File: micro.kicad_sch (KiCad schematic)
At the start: 13 parts, among them J7 USB_C_Receptacle_USB2.0_16P, J8 Conn_01x04_Pin, SW8 SW_Push, U4 ESP32-S3-WROOM-2

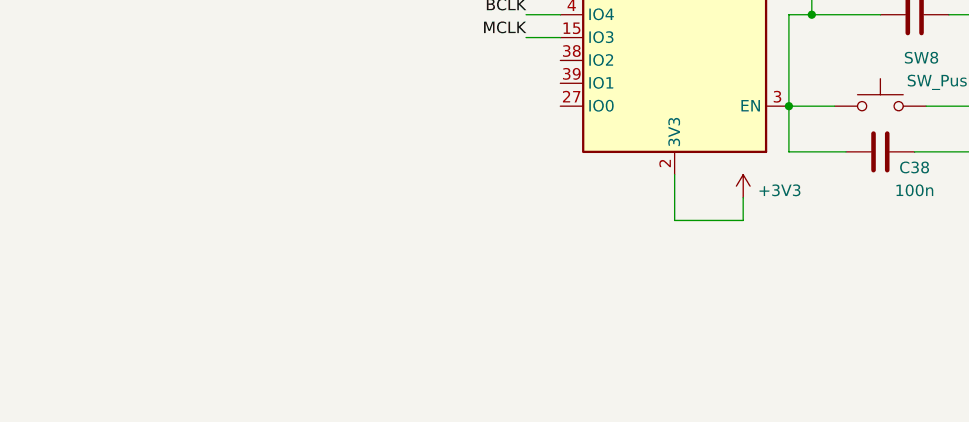
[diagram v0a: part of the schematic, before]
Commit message: aggiunto filtro PLL_LF Adau
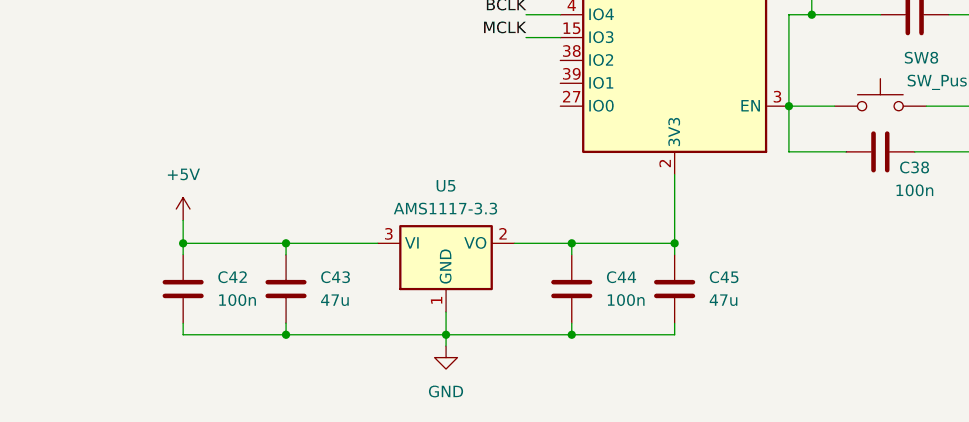
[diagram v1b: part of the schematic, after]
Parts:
- added C42, C44: 100n, Capacitor_SMD:C_0603_1608Metric, symbol Device:C
- added C43, C45: 47u, Capacitor_SMD:C_0603_1608Metric, symbol Device:C
- added U5: AMS1117-3.3, Package_TO_SOT_SMD:SOT-223-3_TabPin2, symbol Regulator_Linear:AMS1117-3.3
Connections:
- net +3V3: no longer U4.2 (3V3)
- net +5V: now also C42.1, C43.1, U5.3 (VI)
- net GND: now also C42.2, C43.2, C44.2, C45.2, U5.1 (GND)
- new net: C44.1, C45.1, U4.2 (3V3), U5.2 (VO)

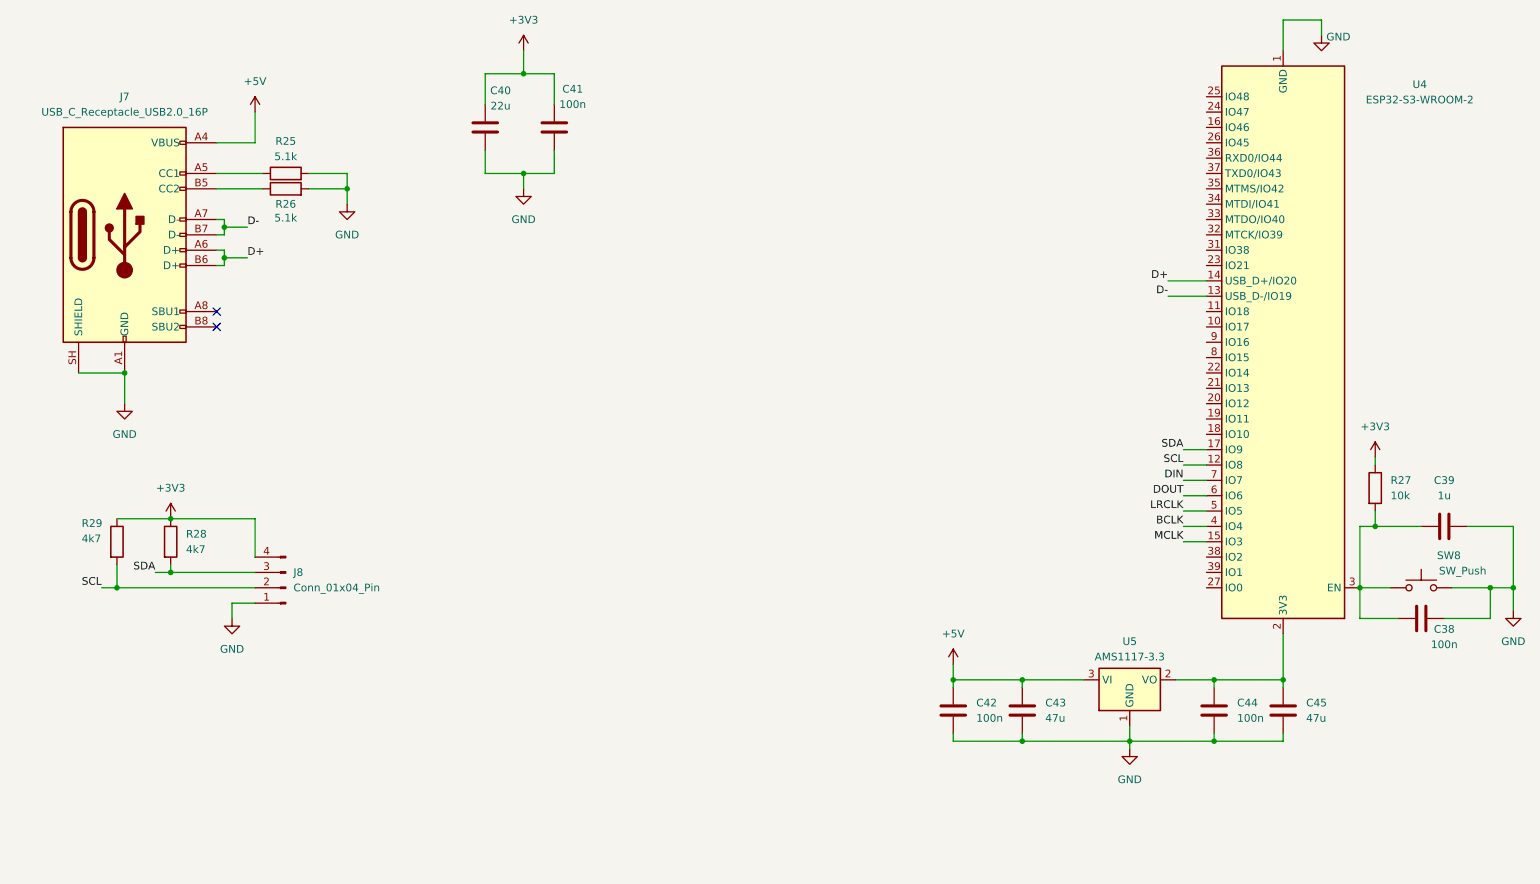
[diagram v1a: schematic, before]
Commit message: sostituito micro esp32 a stm32
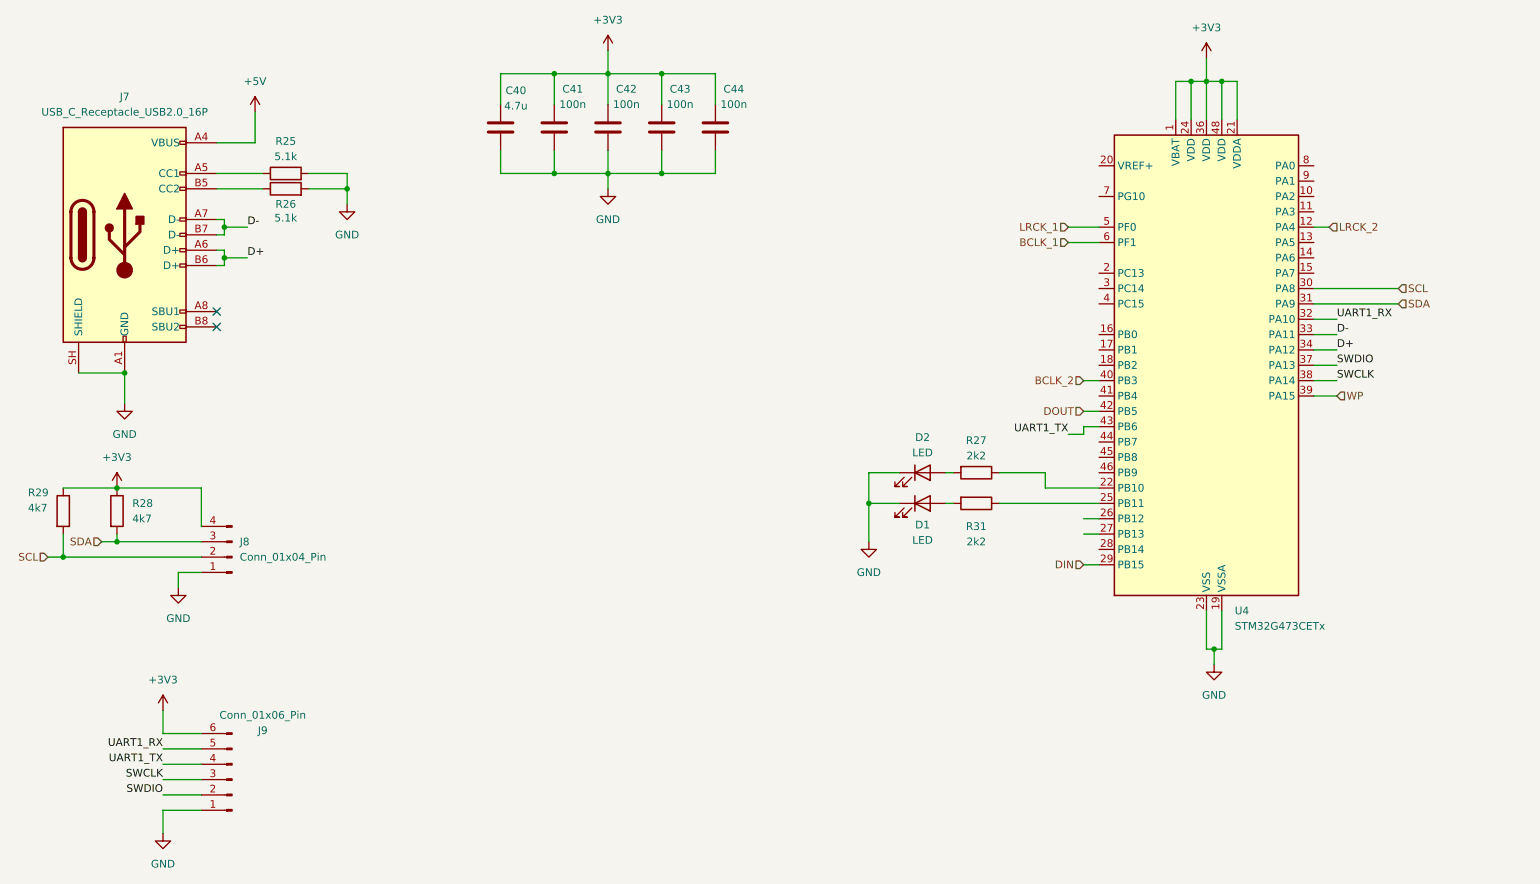
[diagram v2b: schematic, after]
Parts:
- removed C38: 100n, Capacitor_SMD:C_0603_1608Metric, symbol Device:C
- removed C39: 1u, Capacitor_SMD:C_0603_1608Metric, symbol Device:C
- removed C45: 47u, Capacitor_SMD:C_0603_1608Metric, symbol Device:C
- removed SW8: SW_Push, Button_Switch_SMD:SW_SPST_PTS645Sx43SMTR92, symbol Switch:SW_Push
- removed U4: ESP32-S3-WROOM-2, RF_Module:ESP32-S3-WROOM-2, symbol RF_Module:ESP32-S3-WROOM-2
- removed U5: AMS1117-3.3, Package_TO_SOT_SMD:SOT-223-3_TabPin2, symbol Regulator_Linear:AMS1117-3.3
- added D1, D2: LED, LED_SMD:LED_1210_3225Metric, symbol Device:LED
- added J9: Conn_01x06_Pin, Connector_JST:JST_XH_B6B-XH-A_1x06_P2.50mm_Vertical, symbol Connector:Conn_01x06_Pin
- added R31: 2k2, Resistor_SMD:R_0603_1608Metric, symbol Device:R
- added U4: STM32G473CETx, Package_QFP:LQFP-48_7x7mm_P0.5mm, symbol MCU_ST_STM32G4:STM32G473CETx
- C40: value 22u -> 4.7u
- C43: value 47u -> 100n
- R27: value 10k -> 2k2; footprint Capacitor_SMD:C_0603_1608Metric -> Resistor_SMD:R_0603_1608Metric
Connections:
- net +3V3: now also C42.1, C43.1, C44.1, J9.6 (Pin_6), U4.1 (VBAT), U4.21 (VDDA), U4.24 (VDD), U4.36 (VDD), U4.48 (VDD); no longer R27.1
- net +5V: no longer C42.1, C43.1
- net D+: now also U4.34 (PA12)
- net D-: now also U4.33 (PA11)
- net DIN: now also U4.29 (PB15)
- net DOUT: now also U4.42 (PB5)
- net GND: now also D1.1 (K), D2.1 (K), J9.1 (Pin_1), U4.19 (VSSA), U4.23 (VSS), U4.35 (VSS), U4.47 (VSS)
- net SCL: now also U4.30 (PA8)
- net SDA: now also U4.31 (PA9)
- net at R27.2: now also D2.2 (A)
- new net: R27.1, U4.22 (PB10)
- new net: R31.1, U4.25 (PB11)
- new net: D1.2 (A), R31.2
- new net BCLK_1: U4.6 (PF1)
- new net BCLK_2: U4.40 (PB3)
- new net LRCK_1: U4.5 (PF0)
- new net LRCK_2: U4.12 (PA4)
- new net SWCLK: J9.3 (Pin_3), U4.38 (PA14)
- new net SWDIO: J9.2 (Pin_2), U4.37 (PA13)
- new net UART1_RX: J9.5 (Pin_5), U4.32 (PA10)
- new net UART1_TX: J9.4 (Pin_4), U4.43 (PB6)
- new net WP: U4.39 (PA15)
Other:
- moved on the sheet: C40, J8, R28, R29
